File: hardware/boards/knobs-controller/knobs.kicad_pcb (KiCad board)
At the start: 2 copper layers, 110.5 x 54.3 mm, 70 parts, among them J1 ZX62-AB-5PA(31), J4 JST---S4B-PH-SM4-TB(LF)(SN)_J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, J8 2X3_SMD_MALE, SW1 Rotary Encoder, SW2 Rotary Encoder, SW3 Rotary Encoder, U2 AP7215-33YG-13, U3 ATSAMD21G18A-48, Y1 32.768KHz

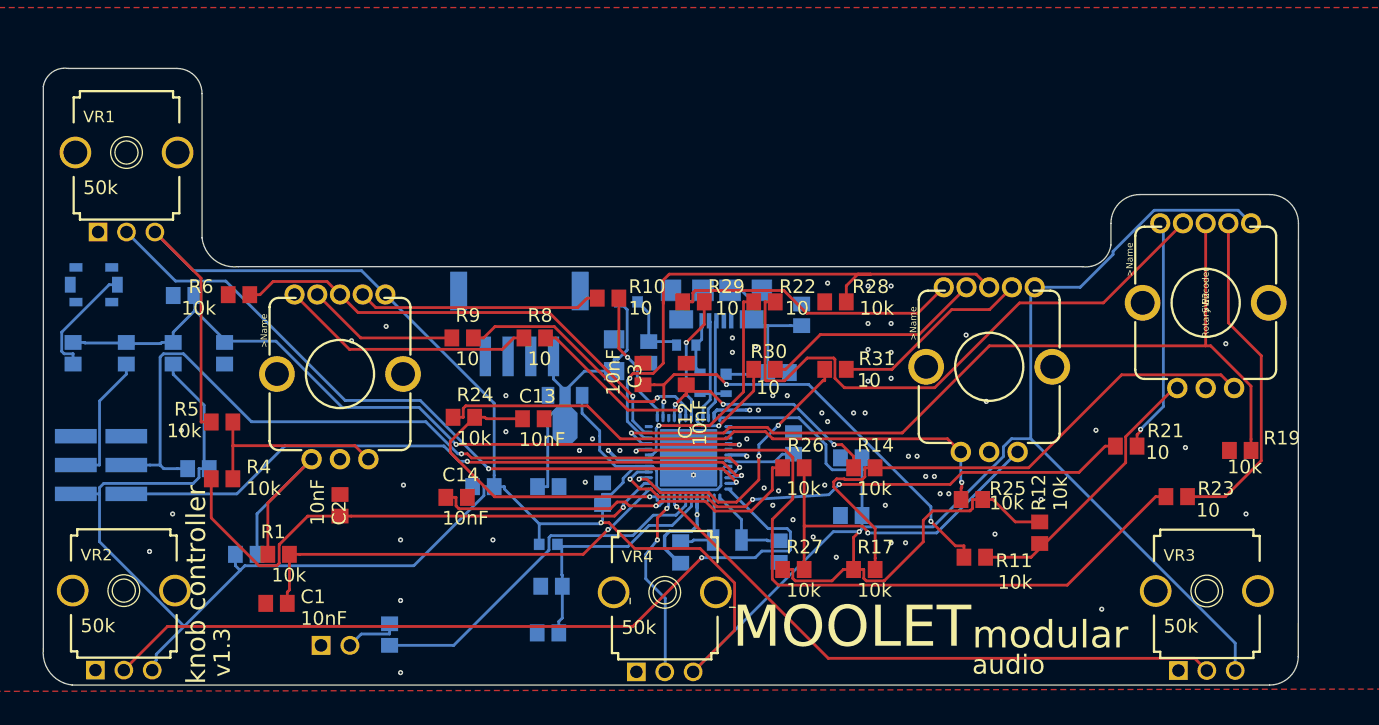
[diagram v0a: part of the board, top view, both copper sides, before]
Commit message: refine knobs board and panel design
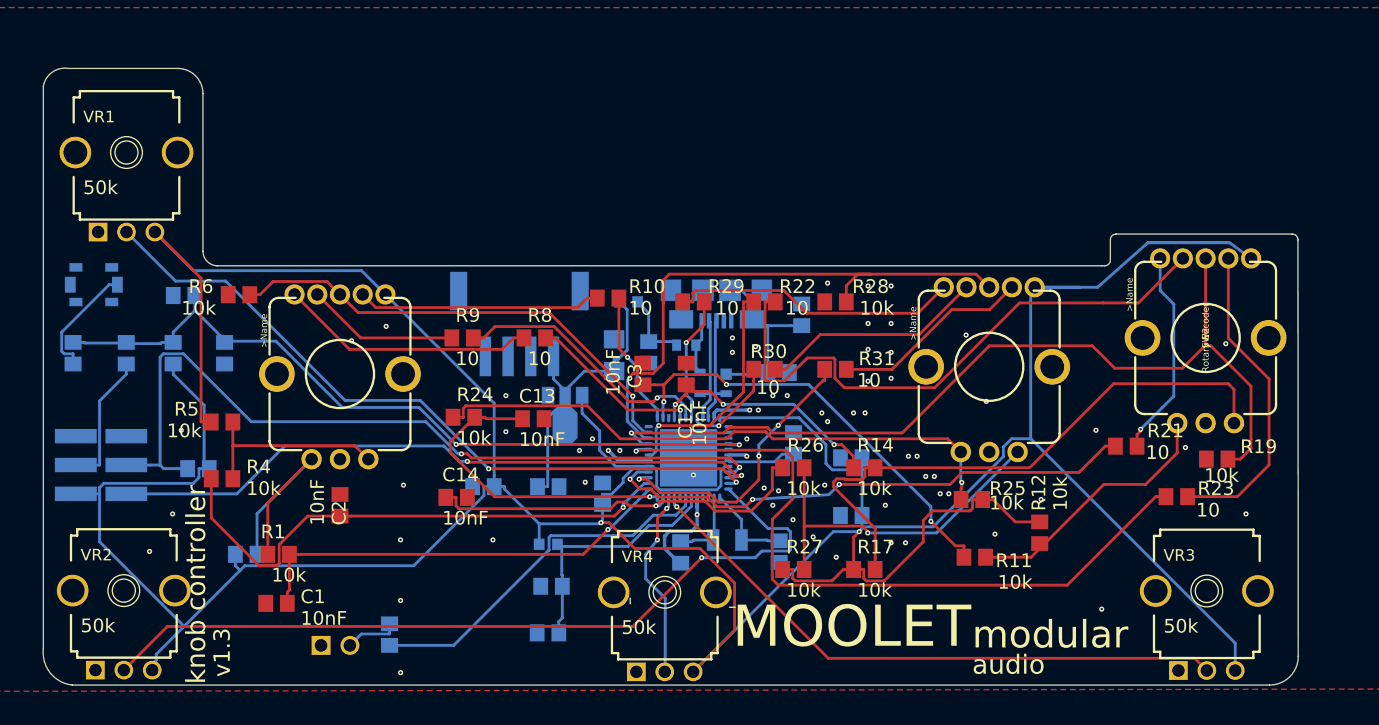
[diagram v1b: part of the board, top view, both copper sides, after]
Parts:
- moved SW2 3.09 mm to (195.6, 101.6)
- moved R19 2.17 mm to (196.6, 112.3)
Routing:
- net +3V3: track 363.2 -> 372.8 mm
- net Net-(R21-Pad1): track 20.7 -> 18.4 mm
- net Net-(R14-Pad2): track 49.4 -> 51.6 mm
- net Net-(R23-Pad1): track 29.9 -> 28.0 mm
- net Net-(R22-Pad1): track 53.5 -> 52.2 mm
- net Net-(R11-Pad1): track 24.8 -> 23.7 mm
- net /knobs_1/PA12_S2_MOSI: track 77.9 -> 78.8 mm
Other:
- outline, holes or cut-outs redrawn

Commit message: asthetics
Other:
- board text added: "v1.4"
- board text removed: "v1.3"

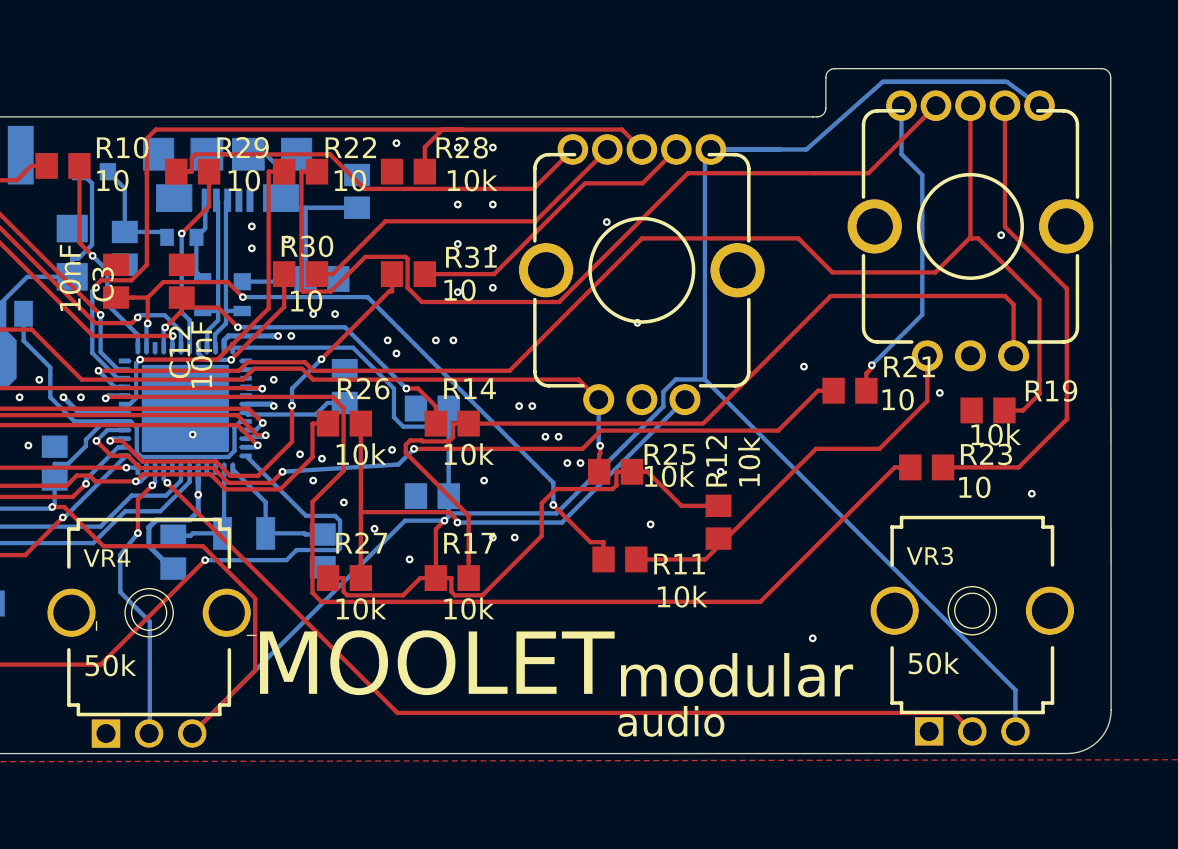
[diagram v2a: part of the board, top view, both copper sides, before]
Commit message: fixed dimentions and step file color
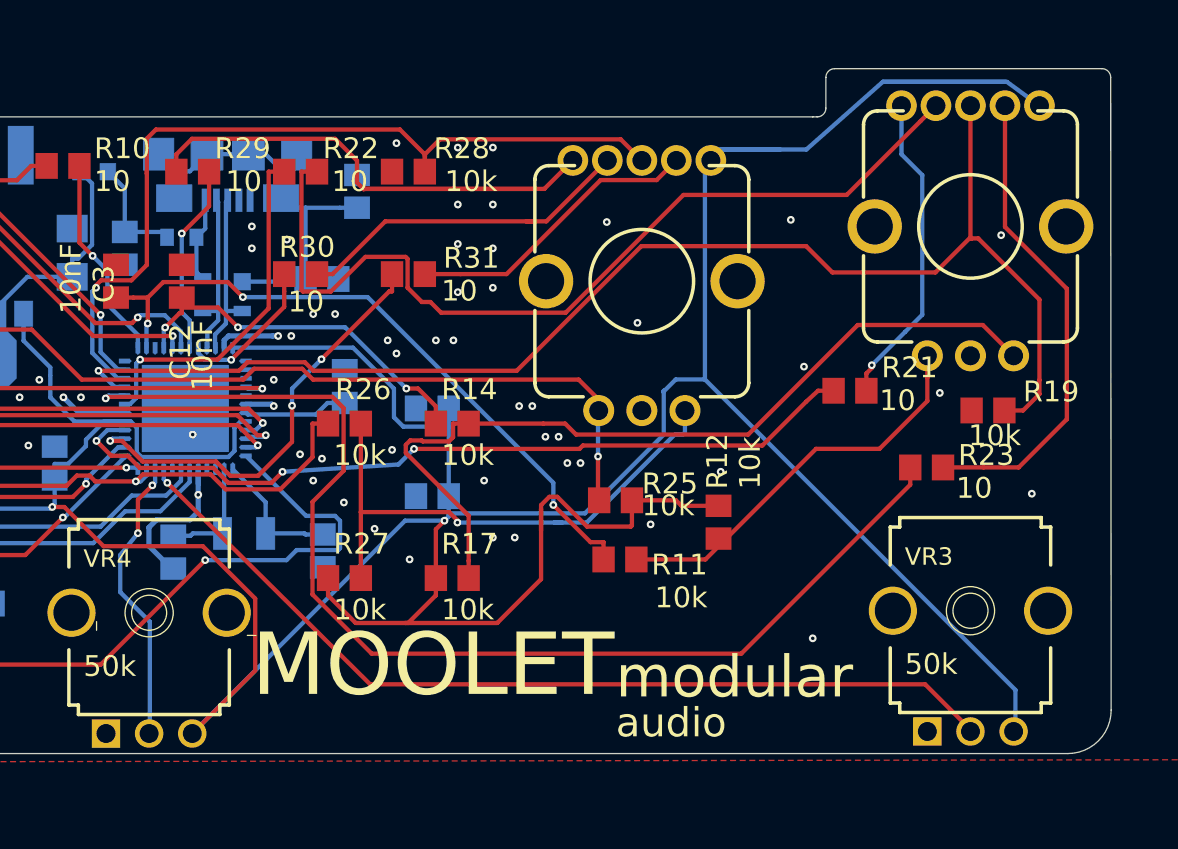
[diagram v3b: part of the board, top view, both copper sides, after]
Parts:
- moved R25 1.65 mm to (175.0, 117.5)
- moved SW3 0.64 mm to (176.5, 104.8)
- moved VR3 0.11 mm to (195.6, 123.9)
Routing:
- net Net-(R29-Pad1): track 25.6 -> 36.8 mm
- net +3V3: track 372.8 -> 380.6 mm
- net /knobs_1/PB11_TCC0-W5: track 64.8 -> 67.9 mm
- net Net-(R14-Pad2): track 51.6 -> 49.1 mm
- net Net-(R24-Pad1): track 52.0 -> 53.0 mm
- net /knobs_1/PA13_S2_SCK: track 50.8 -> 49.8 mm
- net Net-(R26-Pad2): track 31.0 -> 31.9 mm
- net Net-(R22-Pad1): track 52.2 -> 52.7 mm
- net GND: vias 66 -> 67

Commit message: knobs: better alignment of knobs
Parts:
- moved VR2 0.23 mm to (100.6, 123.8)
- moved VR4 0.19 mm to (148.1, 123.8)
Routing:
- net +3V3: track 380.6 -> 378.4 mm
- net GND: vias 67 -> 71
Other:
- board text added: "v1.5"
- board text removed: "v1.4"

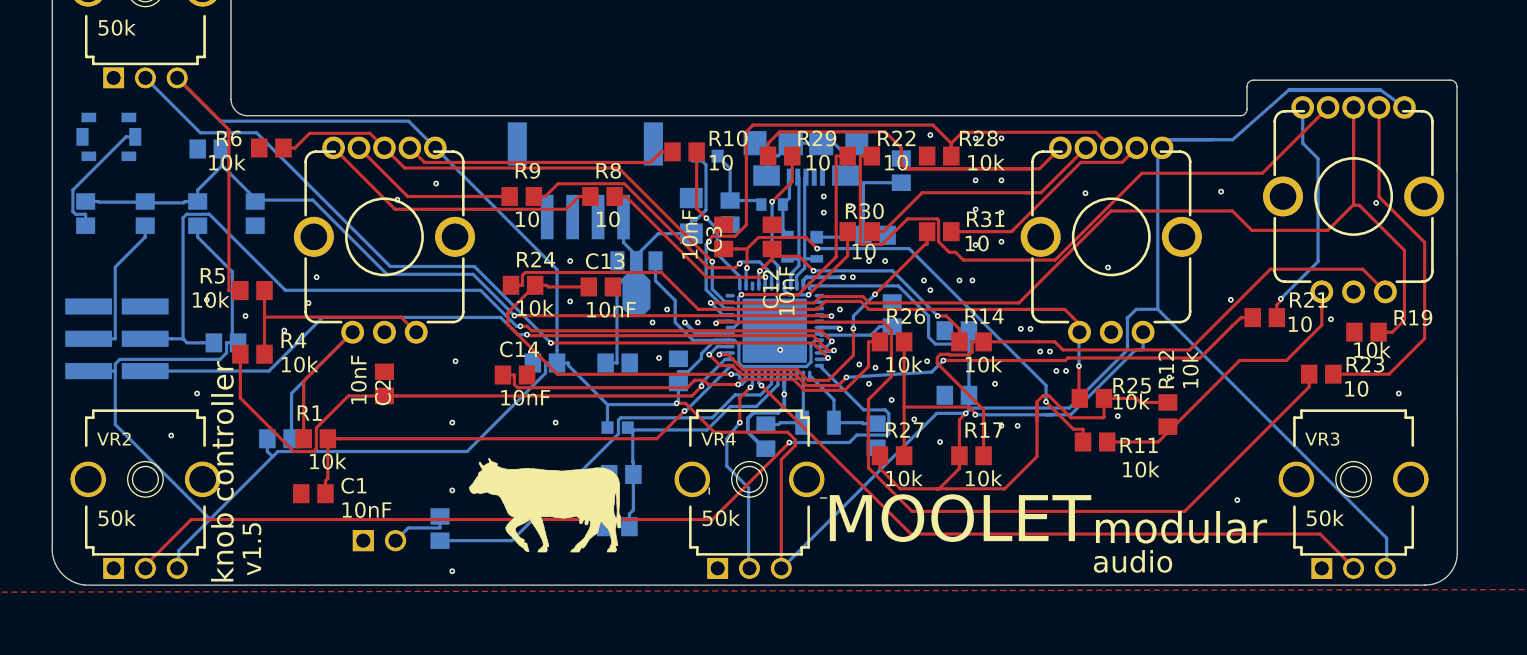
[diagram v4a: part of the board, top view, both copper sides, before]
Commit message: correction: tx, rx connected
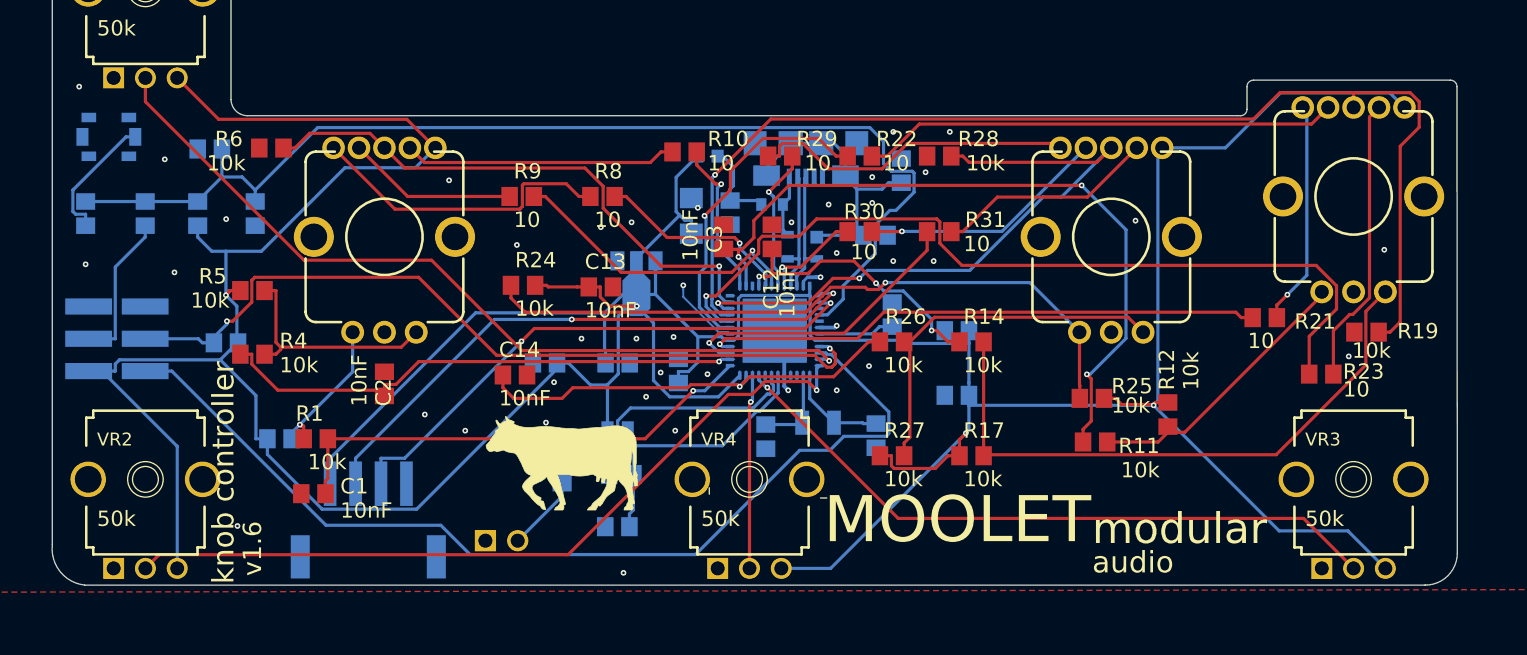
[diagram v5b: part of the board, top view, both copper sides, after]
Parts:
- moved J4 32.7 mm to (118.1, 127.6), turned to 0 degrees
- moved R18 10.6 mm to (133.3, 123.2), turned to -90 degrees
- moved D2 9.60 mm to (128.6, 128.7)
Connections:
- J4 pad 2: (no net) -> /knobs_1/PB23_S5_RX
- J4 pad 3: (no net) -> /knobs_1/PB22_S5_TX
- U3 pad 37: (no net) -> /knobs_1/PB22_S5_TX
- U3 pad 38: (no net) -> /knobs_1/PB23_S5_RX
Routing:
- net +3V3: track 378.4 -> 305.3 mm, vias 2 -> 3
- net /knobs_1/PB22_S5_TX: track 0.00 -> 46.1 mm, vias 0 -> 2
- net /knobs_1/PB23_S5_RX: track 0.00 -> 43.3 mm, vias 0 -> 2
- net VIN: track 25.5 -> 50.0 mm
- net /knobs_1/RESETN: track 67.9 -> 88.9 mm, vias 2 -> 0
- net /knobs_1/PA31_SWDIO: track 58.2 -> 77.5 mm, vias 2 -> 0
- net /knobs_1/PA17_S1_SCK: track 39.6 -> 57.6 mm
- net Net-(R22-Pad1): track 52.7 -> 37.5 mm
- net /knobs_1/PA12_S2_MOSI: track 78.5 -> 91.6 mm
- net /knobs_1/PB08_LED: track 32.5 -> 20.7 mm
- net Net-(R29-Pad1): track 36.8 -> 25.7 mm
- net /knobs_1/PB03_AIN11: track 71.7 -> 61.2 mm
- net Net-(R1-Pad1): track 20.3 -> 11.7 mm, vias 0 -> 1
- net /knobs_1/PA30_SWCLK: track 71.5 -> 63.4 mm
- net /knobs_1/PA09_S0_I2C_SCL: track 47.8 -> 41.8 mm
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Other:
- board text added: "v1.6"
- board text removed: "v1.5"

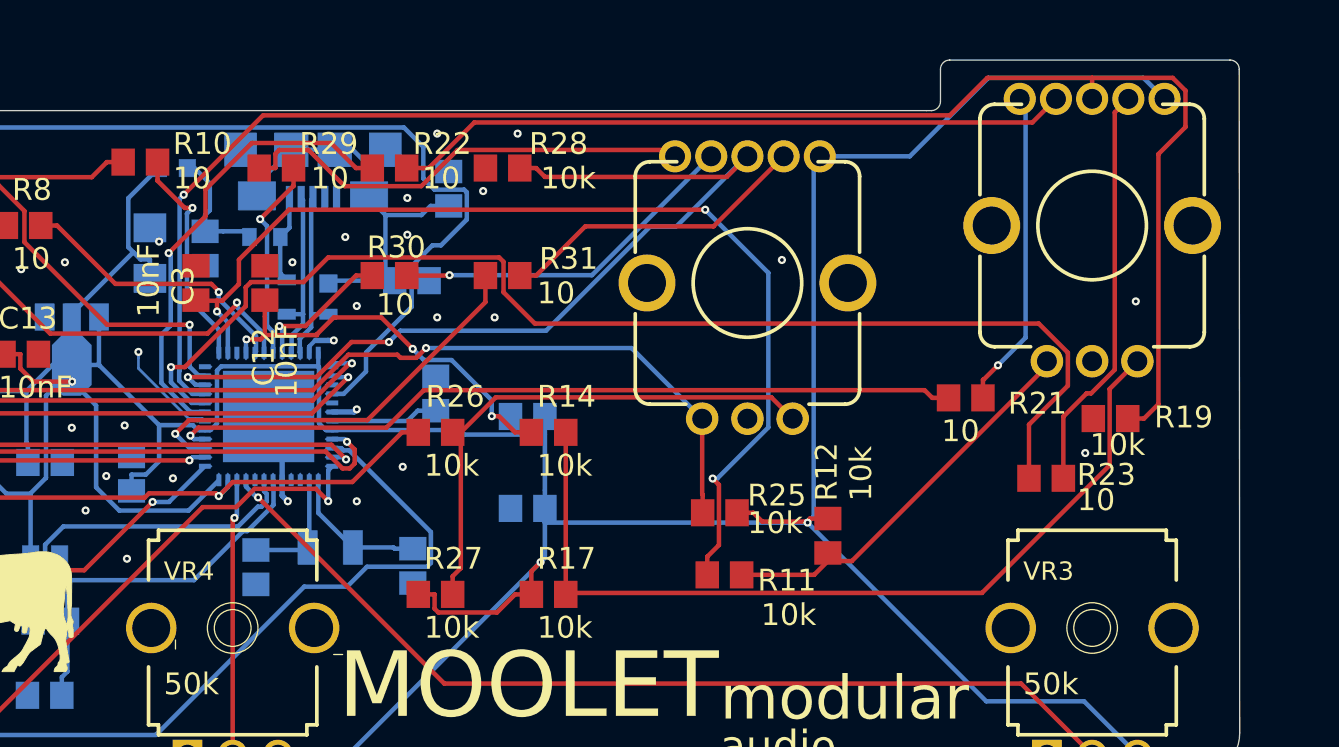
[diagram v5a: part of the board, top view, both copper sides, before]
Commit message: v1.6 minor improvements to knobs- annotated SWD interface and connector to mainboard
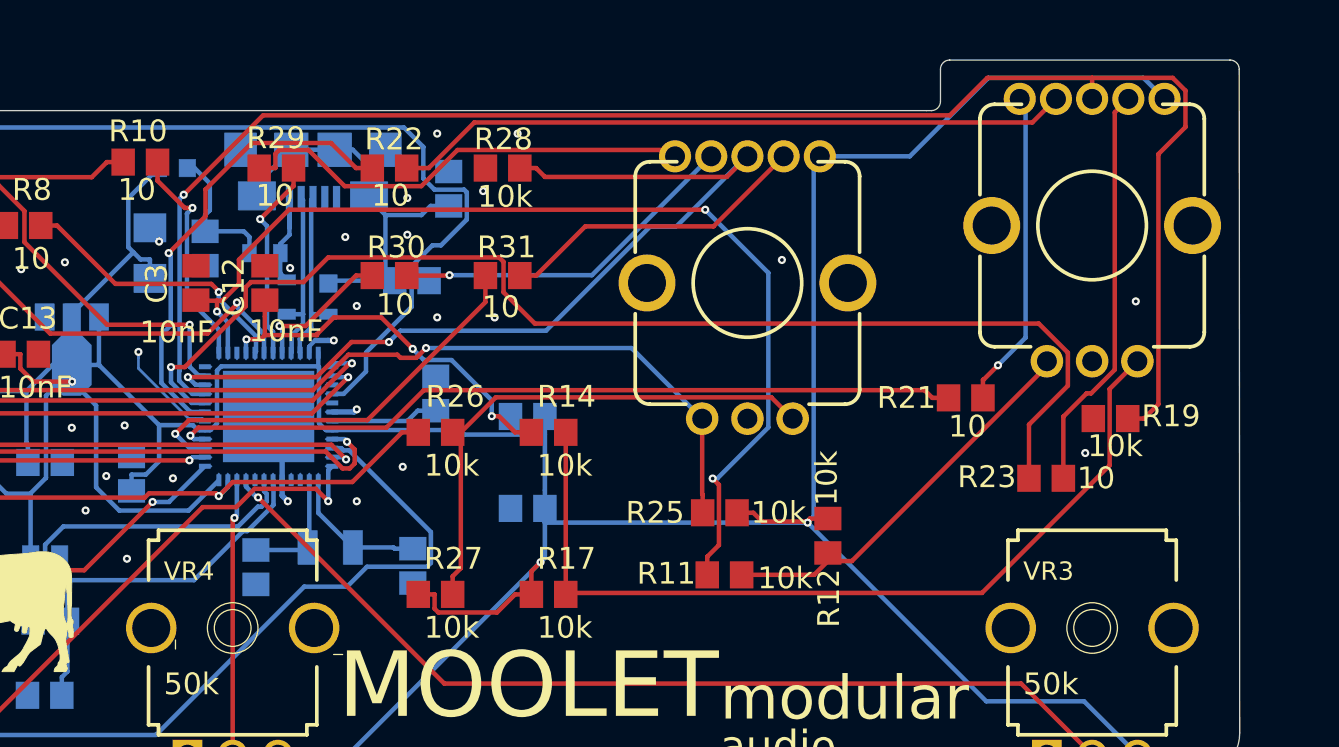
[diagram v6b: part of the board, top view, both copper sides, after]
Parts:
- moved F2 0.89 mm to (149.9, 103.1)
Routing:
- net Net-(D1-Pad4): track 4.88 -> 6.51 mm
- net Net-(C4-Pad1): track 6.93 -> 7.82 mm
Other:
- board text added: "3v3"
- board text added: "GND"
- board text added: "N/C"
- board text added: "RESET"
- board text added: "RX"
- board text added: "SWCLK"
- board text added: "SWDIO"
- board text added: "TX"
- board text added: "VIN (5v)"
